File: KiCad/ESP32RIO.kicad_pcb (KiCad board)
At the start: 4 copper layers, 95 x 65 mm, 40 parts, among them J1 Screw_Terminal_01x12, J2 Screw_Terminal_01x12, U1 PC817, U10 PC817, U11 WeMos_S2_mini, U12 TLP222A, U13 TLP222A, U14 TLP222A, U15 L7805, U16 TLP222A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

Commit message: lagt til bilde av kort
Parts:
- added R17: R, Resistor_THT:R_Axial_DIN0204_L3.6mm_D1.6mm_P2.54mm_Vertical, F.Cu at (119.2, 107.8)
- moved R16 4.21 mm to (119.2, 112.8), turned to 180 degrees
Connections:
- J2 pad 11: GND -> Net-(J2-Pin_11)
- U11 pad 11: unconnected-(U11-GPIO16-Pad11) -> Net-(J2-Pin_11)
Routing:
- net Net-(J2-Pin_12): track 0.00 -> 47.8 mm
- net Net-(J2-Pin_11): track 0.00 -> 45.1 mm
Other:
- board text added: "3AUA Gand VGS Gandsfjorden Gondol RIO Kort V1 2023"
- board text added: "AI2"
- board text added: "BOOT"
- board text added: "Motor + -"
- board text added: "RS-485 A B"
- board text added: "Reset"
- board text removed: "Modbus A B"
- board text removed: "Motor"

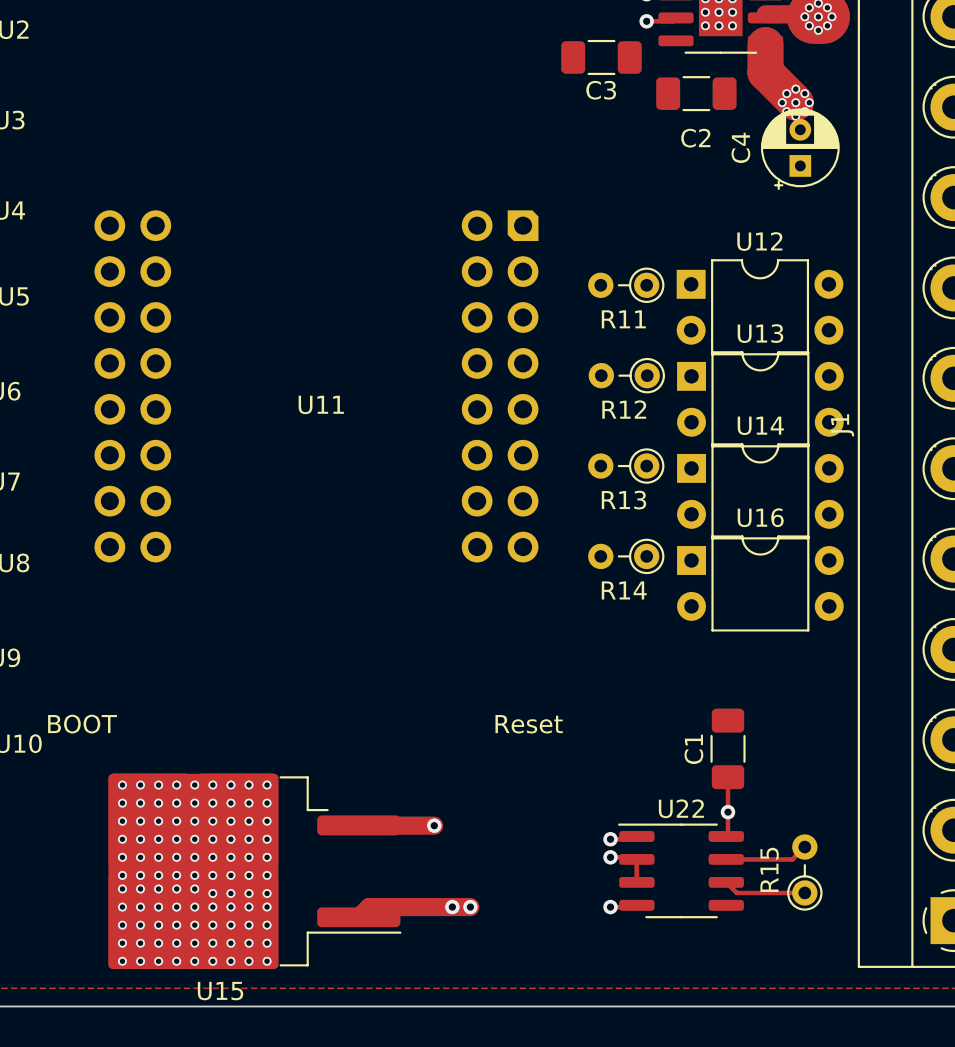
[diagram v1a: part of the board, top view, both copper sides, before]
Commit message: fix kondensator og regulator
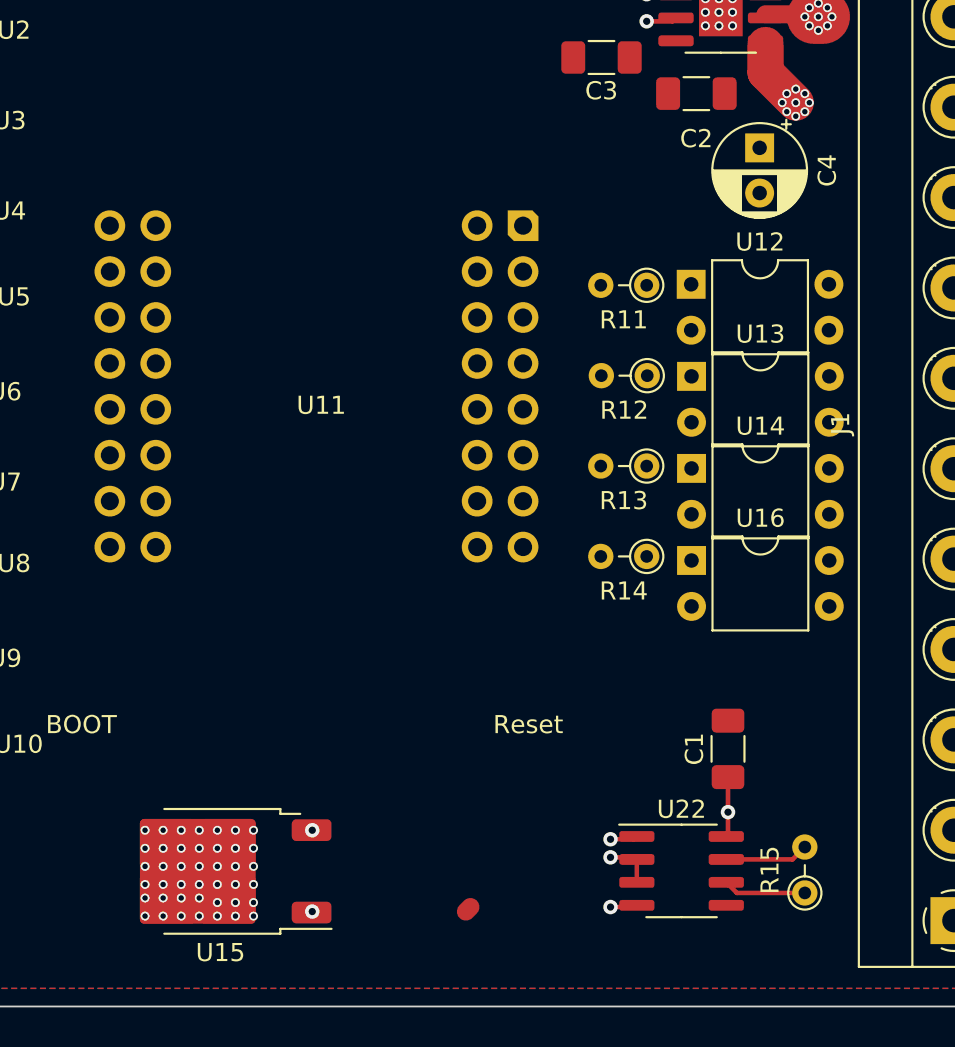
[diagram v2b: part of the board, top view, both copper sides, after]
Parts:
- C4: value 47uF -> 47µF; footprint Capacitor_THT:CP_Radial_D4.0mm_P2.00mm -> Capacitor_THT:CP_Radial_D5.0mm_P2.50mm
- R11: value R -> 120R
- U15: footprint Package_TO_SOT_SMD:TO-263-2 -> Package_TO_SOT_SMD:TO-252-2
- moved C4 2.46 mm to (173.2, 69.5), turned to -90 degrees
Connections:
- C4 pad 1: GND -> Net-(J1-Pin_10)
- C4 pad 2: Net-(J1-Pin_10) -> GND
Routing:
- net Net-(U11-VBUS): track 30.1 -> 20.3 mm
- net +24V: track 37.0 -> 45.2 mm, vias 2 -> 1
- net Net-(J1-Pin_10): track 13.2 -> 16.4 mm
- net GND: vias 111 -> 54
